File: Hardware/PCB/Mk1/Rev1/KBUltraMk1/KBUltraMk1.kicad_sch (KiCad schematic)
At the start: 0 parts

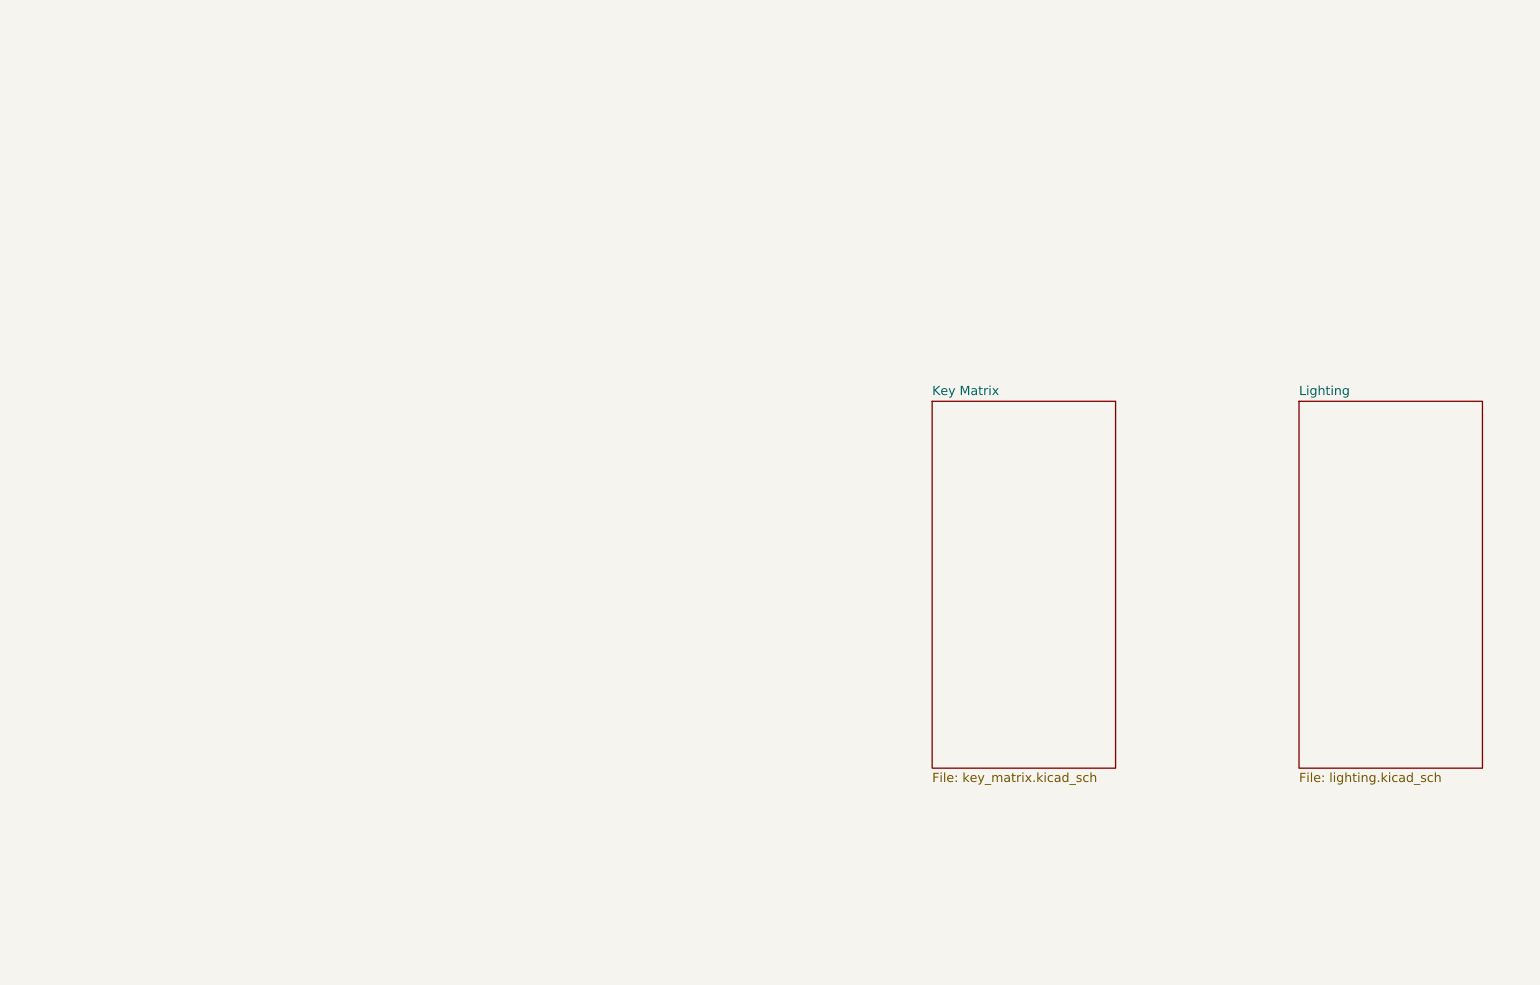
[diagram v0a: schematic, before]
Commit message: Added RP MCU
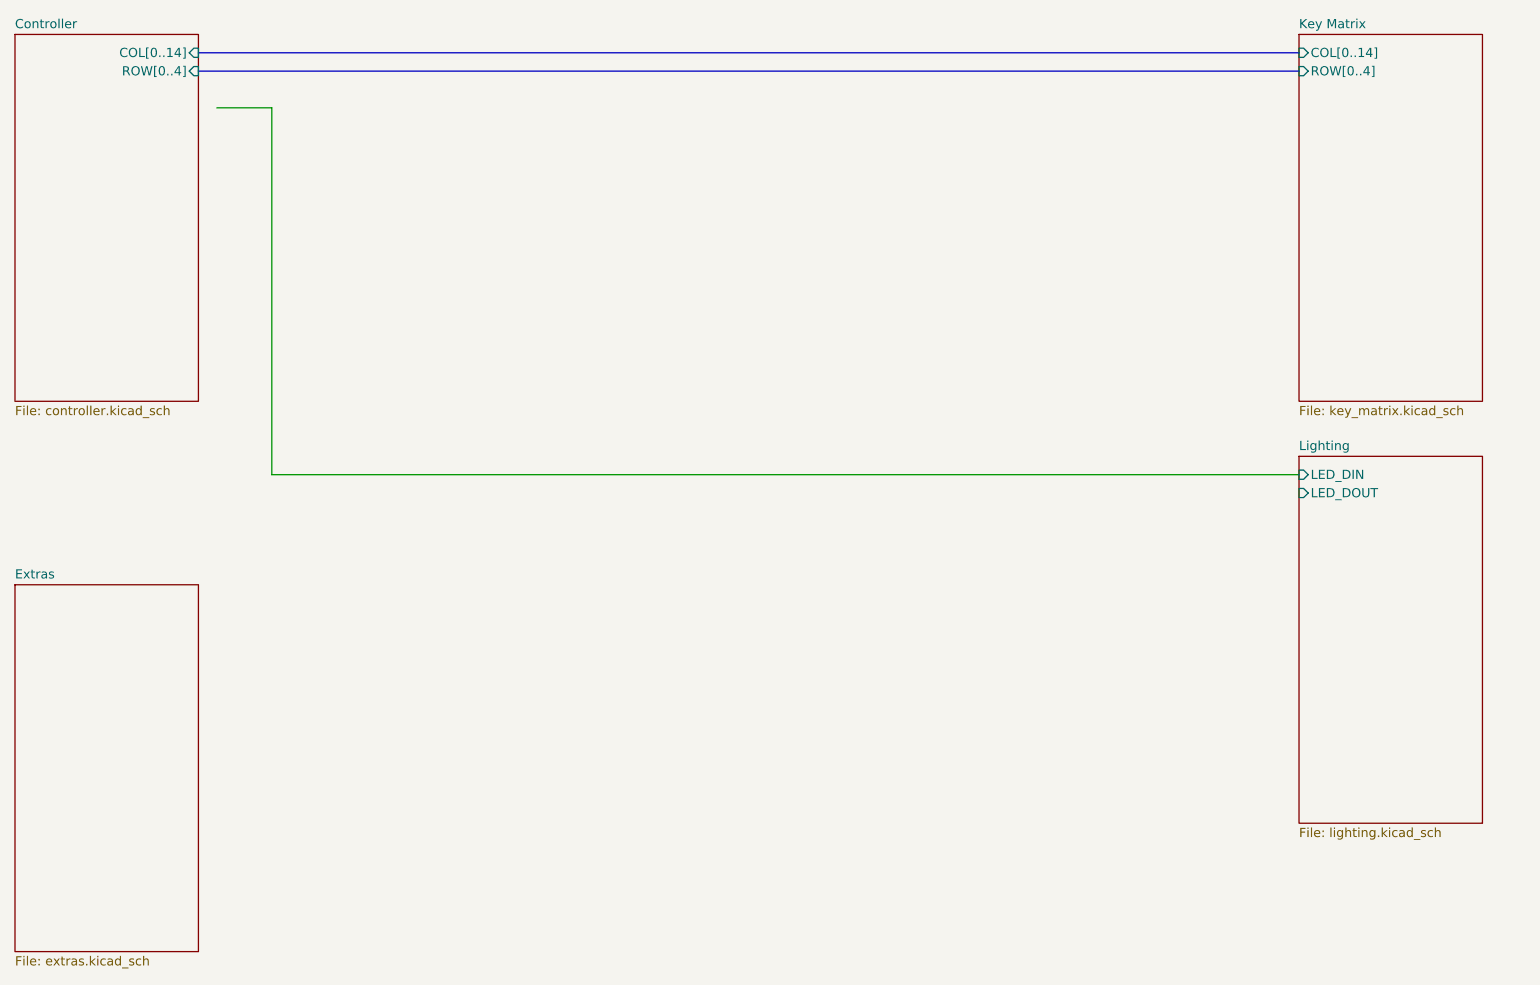
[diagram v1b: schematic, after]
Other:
- added sheet Controller (controller.kicad_sch)
- added sheet Extras (extras.kicad_sch)
- sheet Key Matrix ports: added COL[0..14], ROW[0..4]; removed none
- sheet Lighting ports: added LED_DIN, LED_DOUT; removed none
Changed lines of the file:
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@@
 	(generator "eeschema")
 	(generator_version "10.0")
-	(paper "A3")
-	(sheet
-		(at 177.8 76.2)
+	(paper "A4")
+	(wire
+		(pts
+			(xy 228.6 86.36) (xy 86.36 86.36)
+		)
+		(stroke
+			(width 0)
+			(type default)
+		)
+	)
+	(wire
+		(pts
+			(xy 78.74 35.56) (xy 86.36 35.56)
+		)
+		(stroke
+			(width 0)
+			(type default)
+		)
+	)
+	(bus
+		(pts
+			(xy 76.2 30.48) (xy 228.6 30.48)
+		)
+		(stroke
+			(width 0)
+			(type default)
+		)
+	)
+	(bus
+		(pts
+			(xy 76.2 27.94) (xy 228.6 27.94)
+		)
+		(stroke
+			(width 0)
+			(type default)
+		)
+	)
+	(wire
+		(pts
+			(xy 86.36 86.36) (xy 86.36 35.56)
+		)
+		(stroke
+			(width 0)
+			(type default)
+		)
+	)
+	(sheet
+		(at 228.6 25.4)
 		(size 25.4 50.8)
 		(exclude_from_sim no)
@@
 		)
 		(property "Sheetname" "Key Matrix"
-			(at 177.8 75.4884 0)
+			(at 228.6 24.6884 0)
 			(show_name no)
 			(do_not_autoplace no)
@@
 		)
 		(property "Sheetfile" "key_matrix.kicad_sch"
-			(at 177.8 127.5846 0)
-			(show_name no)
-			(do_not_autoplace no)
-			(effects
-				(font
-					(size 1.27 1.27)
-				)
-				(justify left top)
+			(at 228.6 76.7846 0)
+			(show_name no)
+			(do_not_autoplace no)
+			(effects
+				(font
+					(size 1.27 1.27)
+				)
+				(justify left top)
+			)
+		)
+		(pin "COL[0..14]" input
+			(at 228.6 27.94 180)
+			(effects
+				(font
+					(size 1.27 1.27)
+				)
+				(justify left)
+			)
+		)
+		(pin "ROW[0..4]" input
+			(at 228.6 30.48 180)
+			(effects
+				(font
+					(size 1.27 1.27)
+				)
+				(justify left)
 			)
 		)
@@
 	)
 	(sheet
-		(at 228.6 76.2)
+		(at 50.8 101.6)
+		(size 25.4 50.8)
+		(exclude_from_sim no)
+		(in_bom yes)
+		(on_board yes)
+		(dnp no)
+		(fields_autoplaced yes)
+		(stroke
+			(width 0.1524)
+			(type solid)
+		)
+		(fill
+			(color 255 255 194 1)
+		)
+		(property "Sheetname" "Extras"
+			(at 50.8 100.8884 0)
+			(show_name no)
+			(do_not_autoplace no)
+			(effects
+				(font
+					(size 1.27 1.27)
+				)
+				(justify left bottom)
+			)
+		)
+		(property "Sheetfile" "extras.kicad_sch"
+			(at 50.8 152.9846 0)
+			(show_name no)
+			(do_not_autoplace no)
+			(effects
+				(font
+					(size 1.27 1.27)
+				)
+				(justify left top)
+			)
+		)
+		(instances
+			(project "KBUltraMk1"
+				(path "/b5c66110-c4bc-44b7-b74f-0bc521af7455"
+					(page "5")
+				)
+			)
+		)
+	)
+	(sheet
+		(at 228.6 83.82)
 		(size 25.4 50.8)
 		(exclude_from_sim no)
@@
 		)
 		(property "Sheetname" "Lighting"
-			(at 228.6 75.4884 0)
+			(at 228.6 83.1084 0)
 			(show_name no)
 			(do_not_autoplace no)
@@
 		)
 		(property "Sheetfile" "lighting.kicad_sch"
-			(at 228.6 127.5846 0)
-			(show_name no)
-			(do_not_autoplace no)
-			(effects
-				(font
-					(size 1.27 1.27)
-				)
-				(justify left top)
+			(at 228.6 135.2046 0)
+			(show_name no)
+			(do_not_autoplace no)
+			(effects
+				(font
+					(size 1.27 1.27)
+				)
+				(justify left top)
+			)
+		)
+		(pin "LED_DIN" input
+			(at 228.6 86.36 180)
+			(effects
+				(font
+					(size 1.27 1.27)
+				)
+				(justify left)
+			)
+		)
+		(pin "LED_DOUT" input
+			(at 228.6 88.9 180)
+			(effects
+				(font
+					(size 1.27 1.27)
+				)
+				(justify left)
 			)
 		)
@@
 				)
 			)
+		)
+	)
+	(sheet
+		(at 50.8 25.4)
+		(size 25.4 50.8)
+		(exclude_from_sim no)
+		(in_bom yes)
+		(on_board yes)
+		(dnp no)
+		(fields_autoplaced yes)
+		(stroke
+			(width 0.1524)
+			(type solid)
+		)
+		(fill
+			(color 255 255 194 1)
+		)
+		(property "Sheetname" "Controller"
+			(at 50.8 24.6884 0)
+			(show_name no)
+			(do_not_autoplace no)
+			(effects
+				(font
+					(size 1.27 1.27)
+				)
+				(justify left bottom)
+			)
+		)
+		(property "Sheetfile" "controller.kicad_sch"
+			(at 50.8 76.7846 0)
+			(show_name no)
+			(do_not_autoplace no)
+			(effects
+				(font
+					(size 1.27 1.27)
+				)
+				(justify left top)
+			)
+		)
+		(pin "COL[0..14]" input
+			(at 76.2 27.94 0)
+			(effects
+				(font
+					(size 1.27 1.27)
+				)
+				(justify right)
+			)
+		)
+		(pin "ROW[0..4]" input
+			(at 76.2 30.48 0)
+			(effects
+				(font
+					(size 1.27 1.27)
+				)
+				(justify right)
+			)
+		)
+		(instances
+			(project "KBUltraMk1"
+				(path "/b5c66110-c4bc-44b7-b74f-0bc521af7455"
+					(page "4")
+				)
+			)
